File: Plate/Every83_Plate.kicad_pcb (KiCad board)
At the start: 2 copper layers, 333.6 x 134 mm, 83 parts

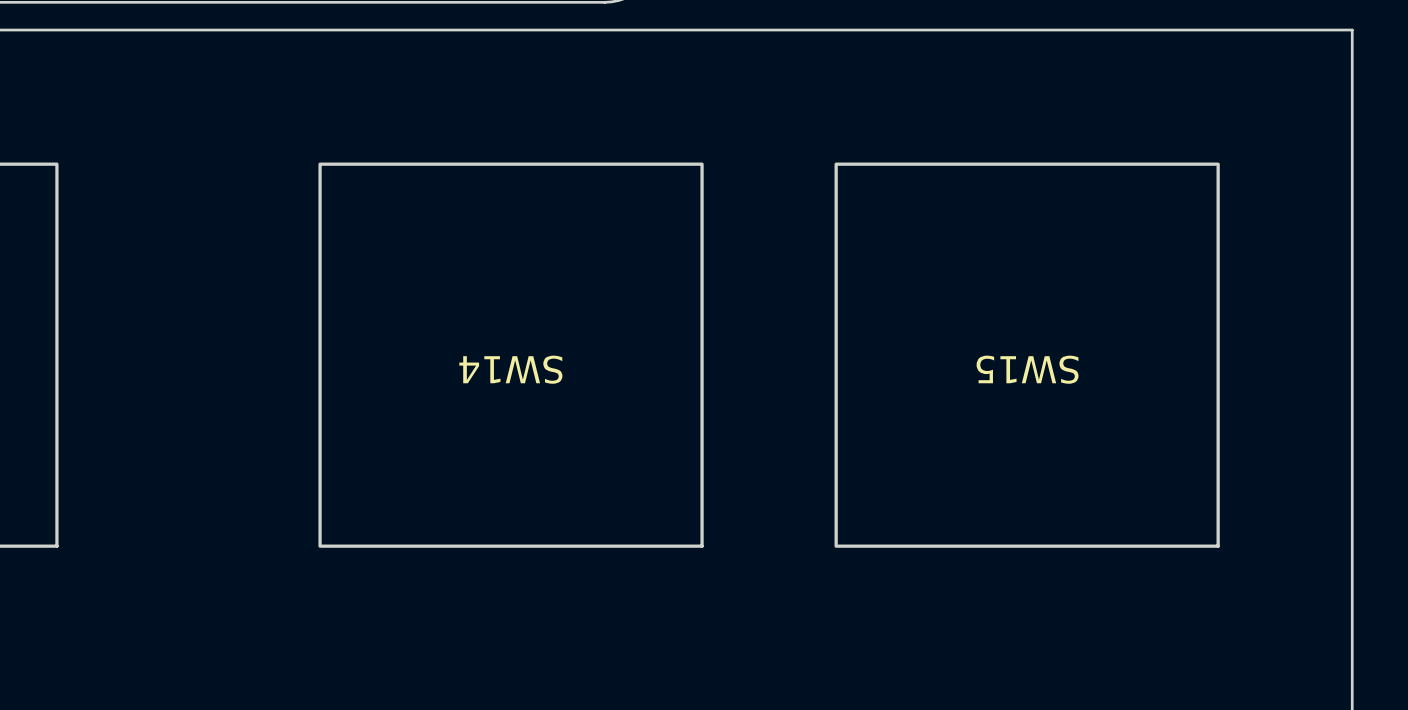
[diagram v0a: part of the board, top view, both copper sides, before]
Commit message: Finalize plate layout
As to whether or not to copper fill, yet to be determined
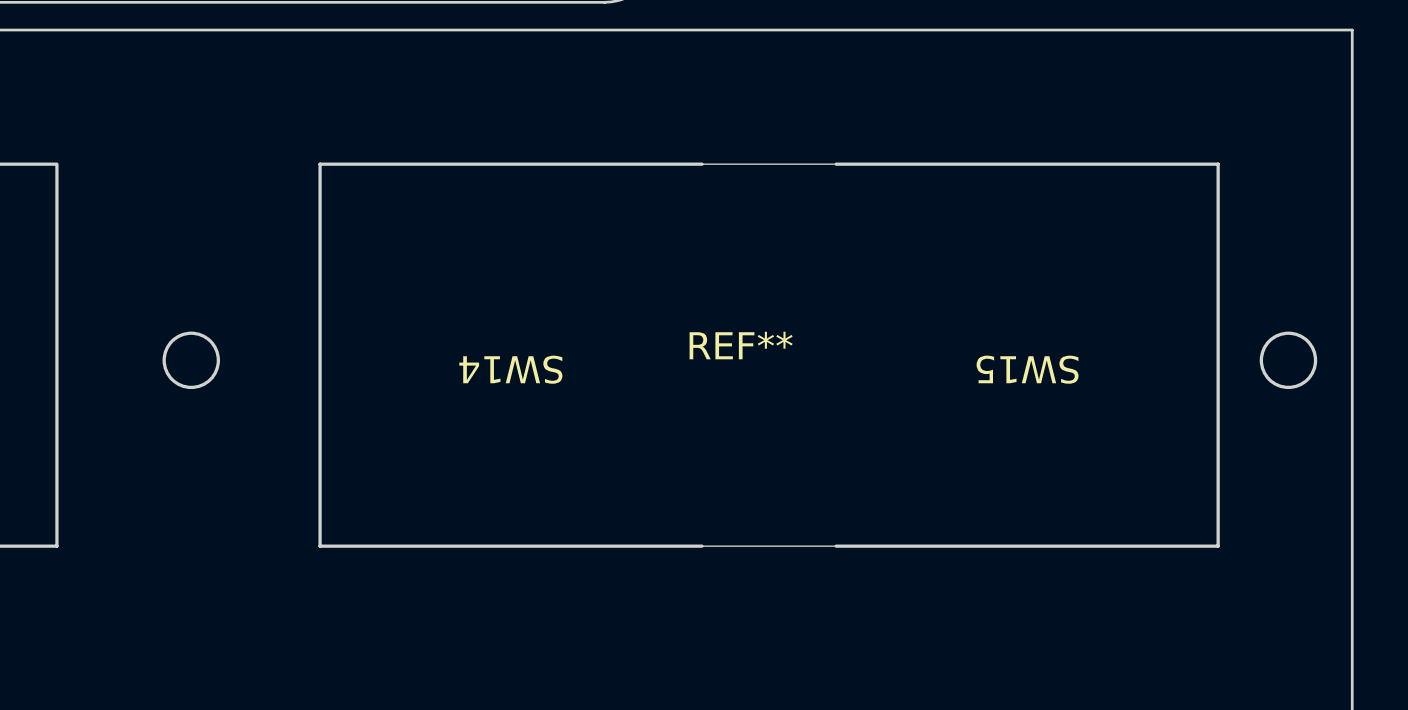
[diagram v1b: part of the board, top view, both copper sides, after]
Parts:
- added REF**: DFR0995_Mounting_holes, JohnDeereLibrary:DFR0995_Mounting_holes, F.Cu at (353.4, 48.5)
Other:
- outline, holes or cut-outs redrawn
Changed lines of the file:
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@@
         (effects (font (size 1 1) (thickness 0.15)))
     )
-    (fp_line (start 12.263 8.628) (end -11.74 8.628)
-      (stroke (width 0.12) (type default)) (layer "Dwgs.User"))
+    (fp_rect (start -12 7.48) (end 12 8.48)
+      (stroke (width 0.12) (type default)) (fill none) (layer "Cmts.User"))
     (fp_line (start -14.93 -5.58) (end -14.93 6.8)
       (stroke (width 0.12) (type default)) (layer "Edge.Cuts"))
@@
     )
   )
+  (footprint "JohnDeereLibrary:DFR0995_Mounting_holes" (layer "F.Cu")
+    (at 353.441 48.514)
+    (fp_text reference "REF**" (at 0 -0.5 unlocked) (layer "F.SilkS")
+        (effects (font (size 1 1) (thickness 0.15)))
+    )
+    (fp_text value "DFR0995_Mounting_holes" (at 0 1 unlocked) (layer "F.Fab")
+        (effects (font (size 1 1) (thickness 0.15)))
+    )
+    (fp_text user "${REFERENCE}" (at 0 2.5 unlocked) (layer "F.Fab")
+        (effects (font (size 1 1) (thickness 0.15)))
+    )
+    (fp_rect (start -22.25 -9.75) (end 22.25 9.75)
+      (stroke (width 0.12) (type default)) (fill none) (layer "Cmts.User"))
+    (fp_rect (start -15.85 -9.55) (end 17.95 9.55)
+      (stroke (width 0.12) (type default)) (fill none) (layer "Cmts.User"))
+    (fp_circle (center -20.25 0) (end -19.25 0)
+      (stroke (width 0.12) (type default)) (fill none) (layer "Edge.Cuts"))
+    (fp_circle (center 20.25 0) (end 21.25 0)
+      (stroke (width 0.12) (type default)) (fill none) (layer "Edge.Cuts"))
+  )
   (footprint "JohnDeereLibrary:Gateron KS33 Plate" (layer "F.Cu")
     (at 83.058 91.186 180)
@@
         (effects (font (size 1 1) (thickness 0.15)))
     )
-    (fp_line (start 12.263 8.628) (end -11.74 8.628)
-      (stroke (width 0.12) (type default)) (layer "Dwgs.User"))
+    (fp_rect (start -12 7.48) (end 12 8.48)
+      (stroke (width 0.12) (type default)) (fill none) (layer "Cmts.User"))
     (fp_line (start -14.93 -5.58) (end -14.93 6.8)
       (stroke (width 0.12) (type default)) (layer "Edge.Cuts"))
@@
         (effects (font (size 1 1) (thickness 0.15)))
     )
-    (fp_rect (start -7.05 -7.05) (end 7.05 7.05)
-      (stroke (width 0.12) (type default)) (fill none) (layer "Edge.Cuts"))
+    (fp_line (start -7.05 -7.05) (end 7.05 -7.05)
+      (stroke (width 0.12) (type default)) (layer "Edge.Cuts"))
+    (fp_line (start 7.05 -7.05) (end 7.05 7.05)
+      (stroke (width 0.12) (type default)) (layer "Edge.Cuts"))
+    (fp_line (start 7.05 7.05) (end -7.05 7.05)
+      (stroke (width 0.12) (type default)) (layer "Edge.Cuts"))
     (model "C:/Users/u4x5sx5/OneDrive-Deere&Co/OneDrive - Deere & Co/Documents/KiCad/7.0/3dmodels/KS-33 Low Profile 2.0.step"
       (offset (xyz 0 0 0))
@@
         (effects (font (size 1 1) (thickness 0.15)))
     )
+    (fp_rect (start -50 7.48) (end 50 8.48)
+      (stroke (width 0.12) (type default)) (fill none) (layer "Cmts.User"))
     (fp_line (start -52.93 -5.58) (end -52.93 6.8)
       (stroke (width 0.12) (type default)) (layer "Edge.Cuts"))
@@
         (effects (font (size 1 1) (thickness 0.15)))
     )
-    (fp_rect (start -7.05 -7.05) (end 7.05 7.05)
-      (stroke (width 0.12) (type default)) (fill none) (layer "Edge.Cuts"))
+    (fp_line (start -7.05 -7.05) (end -7.05 7.05)
+      (stroke (width 0.12) (type default)) (layer "Edge.Cuts"))
+    (fp_line (start -7.05 7.05) (end 7.05 7.05)
+      (stroke (width 0.12) (type default)) (layer "Edge.Cuts"))
+    (fp_line (start 7.05 -7.05) (end -7.05 -7.05)
+      (stroke (width 0.12) (type default)) (layer "Edge.Cuts"))
     (model "C:/Users/u4x5sx5/OneDrive-Deere&Co/OneDrive - Deere & Co/Documents/KiCad/7.0/3dmodels/KS-33 Low Profile 2.0.step"
       (offset (xyz 0 0 0))
@@
         (effects (font (size 1 1) (thickness 0.15)))
     )
-    (fp_line (start 12.263 8.628) (end -11.74 8.628)
-      (stroke (width 0.12) (type default)) (layer "Dwgs.User"))
+    (fp_rect (start -12 7.48) (end 12 8.48)
+      (stroke (width 0.12) (type default)) (fill none) (layer "Cmts.User"))
     (fp_line (start -14.93 -5.58) (end -14.93 6.8)
       (stroke (width 0.12) (type default)) (layer "Edge.Cuts"))
@@
         (effects (font (size 1 1) (thickness 0.15)))
     )
-    (fp_line (start 12.263 8.628) (end -11.74 8.628)
-      (stroke (width 0.12) (type default)) (layer "Dwgs.User"))
+    (fp_rect (start -12 7.48) (end 12 8.48)
+      (stroke (width 0.12) (type default)) (fill none) (layer "Cmts.User"))
     (fp_line (start -14.93 -5.58) (end -14.93 6.8)
       (stroke (width 0.12) (type default)) (layer "Edge.Cuts"))
@@
         (effects (font (size 1 1) (thickness 0.15)))
     )
-    (fp_line (start 12.263 8.628) (end -11.74 8.628)
-      (stroke (width 0.12) (type default)) (layer "Dwgs.User"))
+    (fp_rect (start -12 7.48) (end 12 8.48)
+      (stroke (width 0.12) (type default)) (fill none) (layer "Cmts.User"))
     (fp_line (start -14.93 -5.58) (end -14.93 6.8)
       (stroke (width 0.12) (type default)) (layer "Edge.Cuts"))
@@
   (gr_line (start 292.45175 35.3) (end 315.45175 35.3)
     (stroke (width 0.1) (type default)) (layer "Edge.Cuts"))
+  (gr_line (start 356.9955 55.3735) (end 352.0455 55.3735)
+    (stroke (width 0.05) (type default)) (layer "Edge.Cuts"))
   (gr_line (start 70.07675 31.3) (end 126.07675 31.3)
     (stroke (width 0.1) (type default)) (layer "Edge.Cuts"))
   (gr_arc (start 315.45175 35.3) (mid 315.96275 35.811) (end 315.45175 36.322)
     (stroke (width 0.1) (type default)) (layer "Edge.Cuts"))
+  (gr_line (start 352.0455 41.2735) (end 356.9955 41.2735)
+    (stroke (width 0.05) (type default)) (layer "Edge.Cuts"))
   (gr_arc (start 214.26425 36.322) (mid 213.75325 35.811) (end 214.26425 35.3)
     (stroke (width 0.1) (type default)) (layer "Edge.Cuts"))

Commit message: Fix stab footprint
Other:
- outline, holes or cut-outs redrawn
